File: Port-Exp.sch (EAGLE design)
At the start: 29 parts, among them IC1 MEGA8-P, IC2 317EMP, U1 MAX4762EUB, U2 MAX40077AUA+21-0036K-M

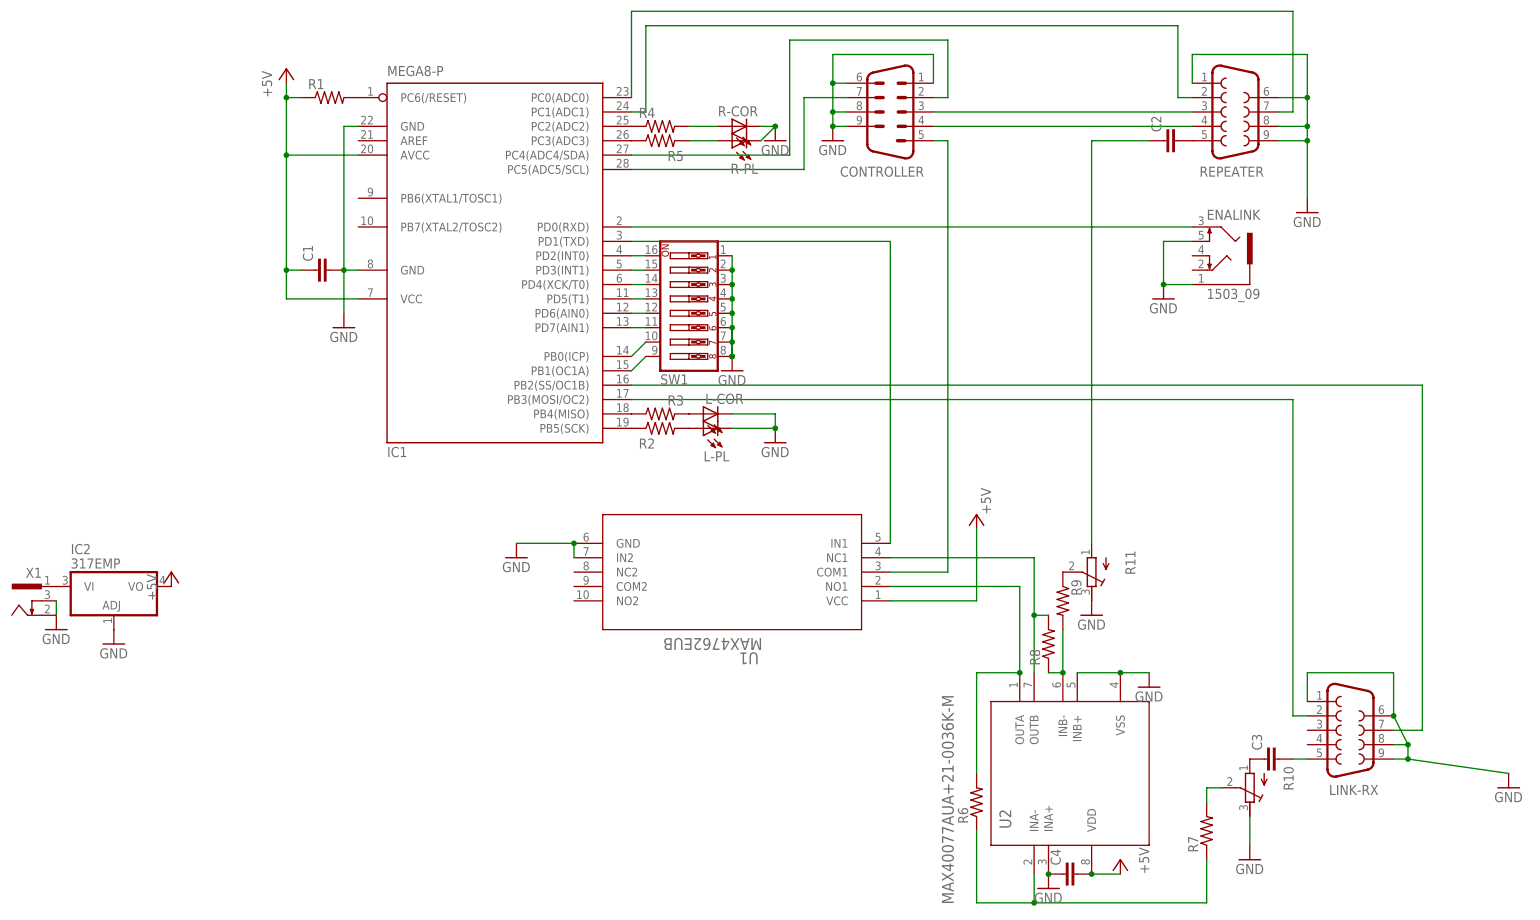
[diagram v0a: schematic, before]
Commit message: tweaked sizes, added label to board, adjusted schematic to print on one sheet
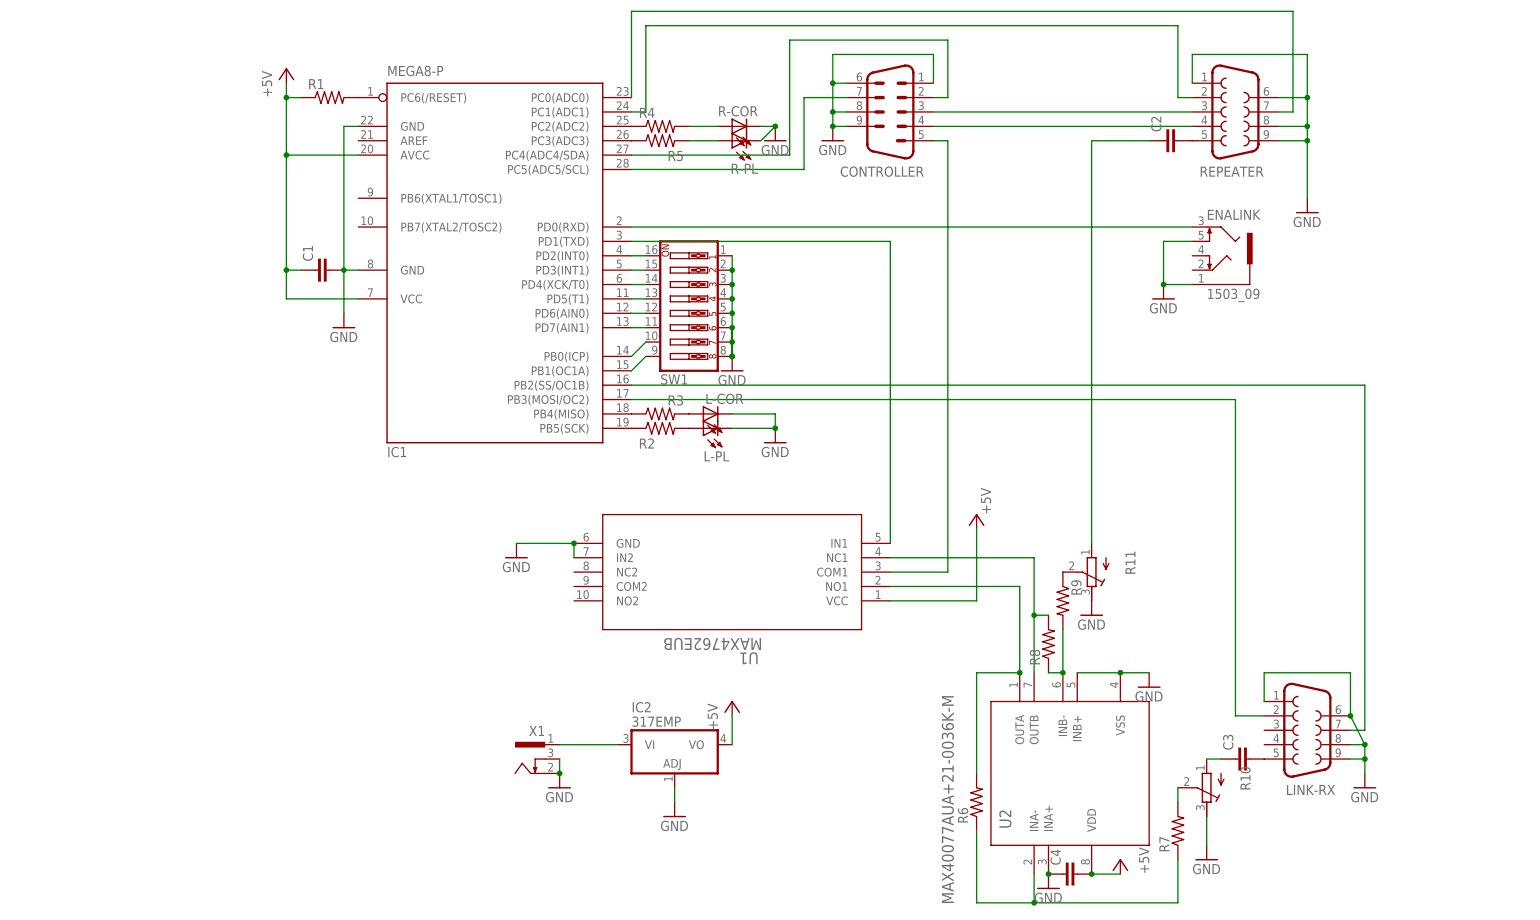
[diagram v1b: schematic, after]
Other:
- moved on the sheet: C3, IC2, LINK-RX, R10, R7, X1
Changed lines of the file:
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@@
 <attribute name="NAME" x="102.87" y="67.31" size="1.778" layer="95"/>
 </instance>
-<instance part="LINK-RX" gate="G$1" x="129.54" y="-30.48" smashed="yes">
-<attribute name="VALUE" x="125.73" y="-41.275" size="1.778" layer="96"/>
-<attribute name="NAME" x="125.73" y="-41.91" size="1.778" layer="95"/>
+<instance part="LINK-RX" gate="G$1" x="121.92" y="-30.48" smashed="yes">
+<attribute name="VALUE" x="118.11" y="-41.275" size="1.778" layer="96"/>
+<attribute name="NAME" x="118.11" y="-41.91" size="1.778" layer="95"/>
 </instance>
 <instance part="CONTROLLER" gate="-1" x="48.26" y="78.74" smashed="yes">
@@
 <instance part="GND1" gate="1" x="38.1" y="73.66"/>
 <instance part="GND2" gate="1" x="121.92" y="60.96"/>
-<instance part="GND3" gate="1" x="157.48" y="-40.64"/>
+<instance part="GND3" gate="1" x="132.08" y="-40.64"/>
 <instance part="IC1" gate="G$1" x="-22.86" y="53.34"/>
 <instance part="GND4" gate="1" x="-48.26" y="40.64"/>
@@
 <attribute name="VALUE" x="66.04" y="7.62" size="1.778" layer="96" rot="R90"/>
 </instance>
-<instance part="P+3" gate="1" x="-78.74" y="-2.54"/>
+<instance part="P+3" gate="1" x="20.32" y="-25.4"/>
 <instance part="GND5" gate="1" x="-17.78" y="0"/>
 <instance part="SW1" gate="A" x="12.7" y="43.18" rot="MR180"/>
@@
 </instance>
 <instance part="C2" gate="G$1" x="96.52" y="73.66" rot="R90"/>
-<instance part="C3" gate="G$1" x="114.3" y="-35.56" rot="R90"/>
+<instance part="C3" gate="G$1" x="109.22" y="-35.56" rot="R90"/>
 <instance part="P+4" gate="1" x="88.9" y="-53.34" smashed="yes">
 <attribute name="VALUE" x="93.98" y="-55.88" size="1.778" layer="96" rot="R90"/>
@@
 <instance part="GND10" gate="1" x="93.98" y="-22.86"/>
 <instance part="R6" gate="G$1" x="63.5" y="-43.18" rot="R90"/>
-<instance part="R7" gate="G$1" x="104.14" y="-48.26" rot="R90"/>
+<instance part="R7" gate="G$1" x="99.06" y="-48.26" rot="R90"/>
 <instance part="R8" gate="G$1" x="76.2" y="-15.24" rot="R90"/>
 <instance part="R9" gate="G$1" x="78.74" y="-7.62" rot="R270"/>
-<instance part="R10" gate="G$1" x="111.76" y="-40.64" rot="R180"/>
+<instance part="R10" gate="G$1" x="104.14" y="-40.64" rot="R180"/>
 <instance part="R11" gate="G$1" x="83.82" y="-2.54" rot="R180"/>
 <instance part="GND11" gate="1" x="83.82" y="-10.16"/>
-<instance part="GND12" gate="1" x="111.76" y="-53.34"/>
-<instance part="X1" gate="G$1" x="-104.14" y="-7.62" rot="MR0"/>
+<instance part="GND12" gate="1" x="104.14" y="-53.34"/>
+<instance part="X1" gate="G$1" x="-15.24" y="-35.56" rot="MR0"/>
 <instance part="ENALINK" gate="G$1" x="106.68" y="53.34"/>
 <instance part="GND13" gate="1" x="96.52" y="45.72"/>
-<instance part="GND14" gate="1" x="-99.06" y="-12.7"/>
-<instance part="GND15" gate="1" x="-88.9" y="-15.24"/>
+<instance part="GND14" gate="1" x="-10.16" y="-40.64"/>
+<instance part="GND15" gate="1" x="10.16" y="-45.72"/>
 <instance part="C4" gate="G$1" x="78.74" y="-55.88" rot="R90"/>
-<instance part="IC2" gate="A1" x="-88.9" y="-7.62"/>
+<instance part="IC2" gate="A1" x="10.16" y="-35.56"/>
 </instances>
 <busses>
@@
 <segment>
 <pinref part="LINK-RX" gate="G$1" pin="1"/>
-<wire x1="121.92" y1="-25.4" x2="121.92" y2="-20.32" width="0.1524" layer="91"/>
+<wire x1="114.3" y1="-25.4" x2="114.3" y2="-20.32" width="0.1524" layer="91"/>
 <pinref part="GND3" gate="1" pin="GND"/>
-<wire x1="121.92" y1="-20.32" x2="137.16" y2="-20.32" width="0.1524" layer="91"/>
-<wire x1="137.16" y1="-20.32" x2="137.16" y2="-27.94" width="0.1524" layer="91"/>
+<wire x1="114.3" y1="-20.32" x2="129.54" y2="-20.32" width="0.1524" layer="91"/>
+<wire x1="129.54" y1="-20.32" x2="129.54" y2="-27.94" width="0.1524" layer="91"/>
 <pinref part="LINK-RX" gate="G$1" pin="9"/>
-<wire x1="139.7" y1="-35.56" x2="157.48" y2="-38.1" width="0.1524" layer="91"/>
-<wire x1="137.16" y1="-35.56" x2="139.7" y2="-35.56" width="0.1524" layer="91"/>
-<wire x1="139.7" y1="-35.56" x2="139.7" y2="-33.02" width="0.1524" layer="91"/>
+<wire x1="132.08" y1="-35.56" x2="132.08" y2="-38.1" width="0.1524" layer="91"/>
+<wire x1="129.54" y1="-35.56" x2="132.08" y2="-35.56" width="0.1524" layer="91"/>
+<wire x1="132.08" y1="-35.56" x2="132.08" y2="-33.02" width="0.1524" layer="91"/>
 <pinref part="LINK-RX" gate="G$1" pin="8"/>
-<wire x1="137.16" y1="-33.02" x2="139.7" y2="-33.02" width="0.1524" layer="91"/>
-<wire x1="139.7" y1="-33.02" x2="137.16" y2="-27.94" width="0.1524" layer="91"/>
+<wire x1="129.54" y1="-33.02" x2="132.08" y2="-33.02" width="0.1524" layer="91"/>
+<wire x1="132.08" y1="-33.02" x2="129.54" y2="-27.94" width="0.1524" layer="91"/>
 <pinref part="LINK-RX" gate="G$1" pin="6"/>
-<junction x="137.16" y="-27.94"/>
-<junction x="139.7" y="-33.02"/>
-<junction x="139.7" y="-35.56"/>
+<junction x="129.54" y="-27.94"/>
+<junction x="132.08" y="-33.02"/>
+<junction x="132.08" y="-35.56"/>
 </segment>
 <segment>
@@
 <pinref part="R10" gate="G$1" pin="E"/>
 <pinref part="GND12" gate="1" pin="GND"/>
-<wire x1="111.76" y1="-45.72" x2="111.76" y2="-50.8" width="0.1524" layer="91"/>
+<wire x1="104.14" y1="-45.72" x2="104.14" y2="-50.8" width="0.1524" layer="91"/>
 </segment>
 <segment>
@@
 <pinref part="GND14" gate="1" pin="GND"/>
 <pinref part="X1" gate="G$1" pin="3"/>
-<wire x1="-99.06" y1="-7.62" x2="-99.06" y2="-10.16" width="0.1524" layer="91"/>
+<wire x1="-10.16" y1="-35.56" x2="-10.16" y2="-38.1" width="0.1524" layer="91"/>
+<junction x="-10.16" y="-38.1"/>
 </segment>
 <segment>
 <pinref part="IC2" gate="A1" pin="ADJ"/>
 <pinref part="GND15" gate="1" pin="GND"/>
+<wire x1="10.16" y1="-40.64" x2="10.16" y2="-43.18" width="0.1524" layer="91"/>
 </segment>
 </net>
@@
 <net name="N$9" class="0">
 <segment>
-<wire x1="142.24" y1="30.48" x2="142.24" y2="-30.48" width="0.1524" layer="91"/>
+<wire x1="132.08" y1="30.48" x2="132.08" y2="-30.48" width="0.1524" layer="91"/>
 <pinref part="LINK-RX" gate="G$1" pin="7"/>
-<wire x1="142.24" y1="-30.48" x2="137.16" y2="-30.48" width="0.1524" layer="91"/>
-<wire x1="2.54" y1="30.48" x2="142.24" y2="30.48" width="0.1524" layer="91"/>
+<wire x1="132.08" y1="-30.48" x2="129.54" y2="-30.48" width="0.1524" layer="91"/>
+<wire x1="2.54" y1="30.48" x2="132.08" y2="30.48" width="0.1524" layer="91"/>
 <pinref part="IC1" gate="G$1" pin="PB2(SS/OC1B)"/>
 </segment>
@@
 <net name="N$3" class="0">
 <segment>
-<wire x1="119.38" y1="27.94" x2="119.38" y2="-27.94" width="0.1524" layer="91"/>
+<wire x1="109.22" y1="27.94" x2="109.22" y2="-27.94" width="0.1524" layer="91"/>
 <pinref part="LINK-RX" gate="G$1" pin="2"/>
-<wire x1="119.38" y1="-27.94" x2="121.92" y2="-27.94" width="0.1524" layer="91"/>
-<wire x1="119.38" y1="27.94" x2="2.54" y2="27.94" width="0.1524" layer="91"/>
+<wire x1="109.22" y1="-27.94" x2="114.3" y2="-27.94" width="0.1524" layer="91"/>
+<wire x1="109.22" y1="27.94" x2="2.54" y2="27.94" width="0.1524" layer="91"/>
 <pinref part="IC1" gate="G$1" pin="PB3(MOSI/OC2)"/>
 </segment>
@@
 <pinref part="IC2" gate="A1" pin="VO"/>
 <pinref part="P+3" gate="1" pin="+5V"/>
+<wire x1="20.32" y1="-27.94" x2="20.32" y2="-33.02" width="0.1524" layer="91"/>
 </segment>
 </net>
@@
 <pinref part="LINK-RX" gate="G$1" pin="5"/>
 <pinref part="C3" gate="G$1" pin="2"/>
-<wire x1="119.38" y1="-35.56" x2="121.92" y2="-35.56" width="0.1524" layer="91"/>
 </segment>
 </net>
@@
 <wire x1="63.5" y1="-60.96" x2="73.66" y2="-60.96" width="0.1524" layer="91"/>
 <wire x1="73.66" y1="-60.96" x2="73.66" y2="-55.88" width="0.1524" layer="91"/>
-<wire x1="73.66" y1="-60.96" x2="104.14" y2="-60.96" width="0.1524" layer="91"/>
+<wire x1="73.66" y1="-60.96" x2="99.06" y2="-60.96" width="0.1524" layer="91"/>
 <pinref part="R7" gate="G$1" pin="1"/>
-<wire x1="104.14" y1="-60.96" x2="104.14" y2="-53.34" width="0.1524" layer="91"/>
+<wire x1="99.06" y1="-60.96" x2="99.06" y2="-53.34" width="0.1524" layer="91"/>
 <junction x="73.66" y="-60.96"/>
 </segment>
@@
 <pinref part="C3" gate="G$1" pin="1"/>
 <pinref part="R10" gate="G$1" pin="A"/>
+<wire x1="104.14" y1="-35.56" x2="106.68" y2="-35.56" width="0.1524" layer="91"/>
 </segment>
 </net>
@@
 <pinref part="R7" gate="G$1" pin="2"/>
 <pinref part="R10" gate="G$1" pin="S"/>
-<wire x1="104.14" y1="-43.18" x2="104.14" y2="-40.64" width="0.1524" layer="91"/>
-<wire x1="104.14" y1="-40.64" x2="106.68" y2="-40.64" width="0.1524" layer="91"/>
+<wire x1="99.06" y1="-43.18" x2="99.06" y2="-40.64" width="0.1524" layer="91"/>
 </segment>
 </net>
@@
 <pinref part="X1" gate="G$1" pin="1"/>
 <pinref part="IC2" gate="A1" pin="VI"/>
-</segment>
-</net>
+<wire x1="0" y1="-33.02" x2="-10.16" y2="-33.02" width="0.1524" layer="91"/>
+</segment>
+</net>
